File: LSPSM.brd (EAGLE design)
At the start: 95.5 x 90.3 mm, 165 parts, among them IC1 ATmega328P, IC10 TMP102, IC11 TMP102, IC2 ATMEGA16U2-MU, IC3 LTC3115, IC4 LTC4078, IC5 MAX17043G+U, IC6 MAX4372F, IC7 LTC3536, IC8 MAX4372F, IC9 LTC3536, Q1 RJU003N03 N-MOSFET, Q2 RJU003N03 N-MOSFET, Q4 RJU003N03 N-MOSFET, Q5 RJU003N03 N-MOSFET, Q6 RJU003N03 N-MOSFET, Q7 RJU003N03 N-MOSFET, Q8 RJU003N03 N-MOSFET, Q9 RJU003N03 N-MOSFET, SW1 RESET, SW2 SWITCH-SPDT

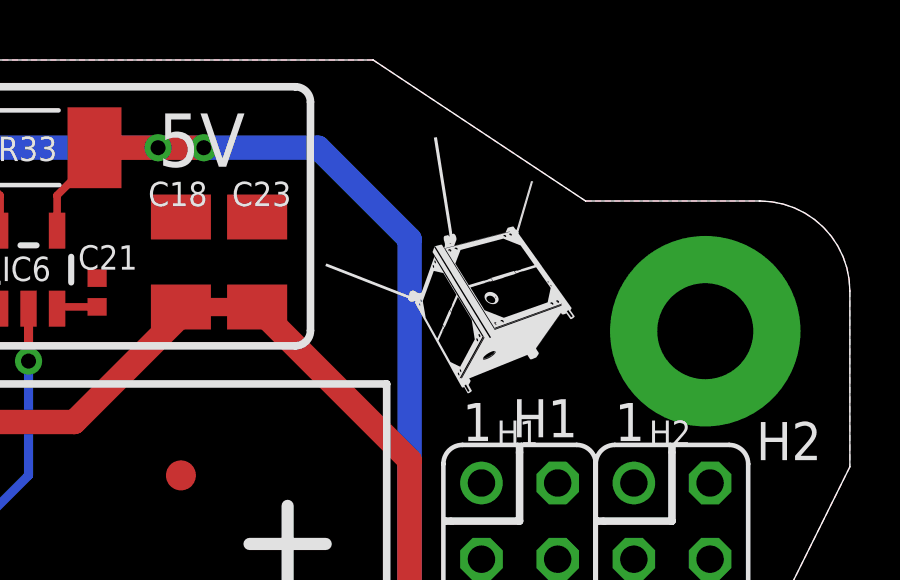
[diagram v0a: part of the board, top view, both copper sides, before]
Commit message: Removed ArduSat logo from silkscreen
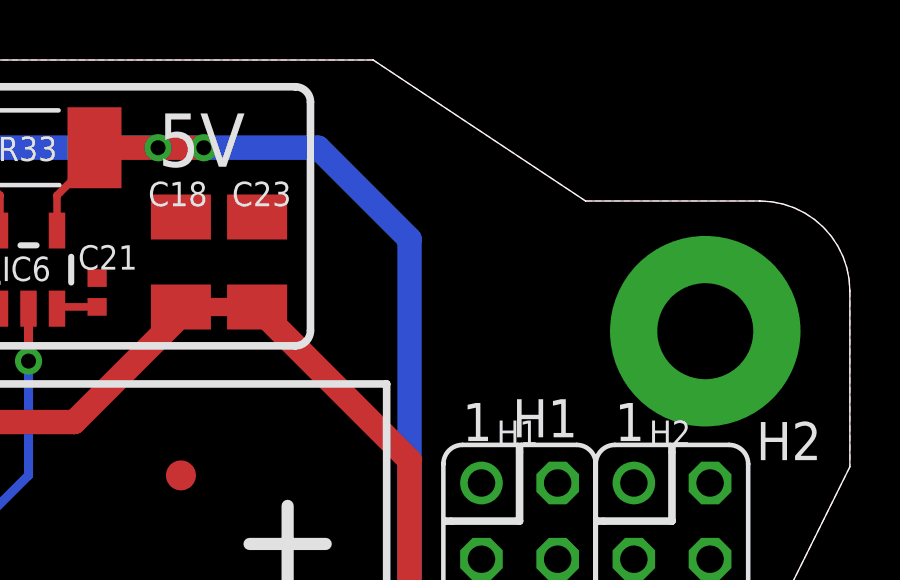
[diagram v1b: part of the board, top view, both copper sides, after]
